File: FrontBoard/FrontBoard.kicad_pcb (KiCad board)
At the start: 2 copper layers, 0 parts

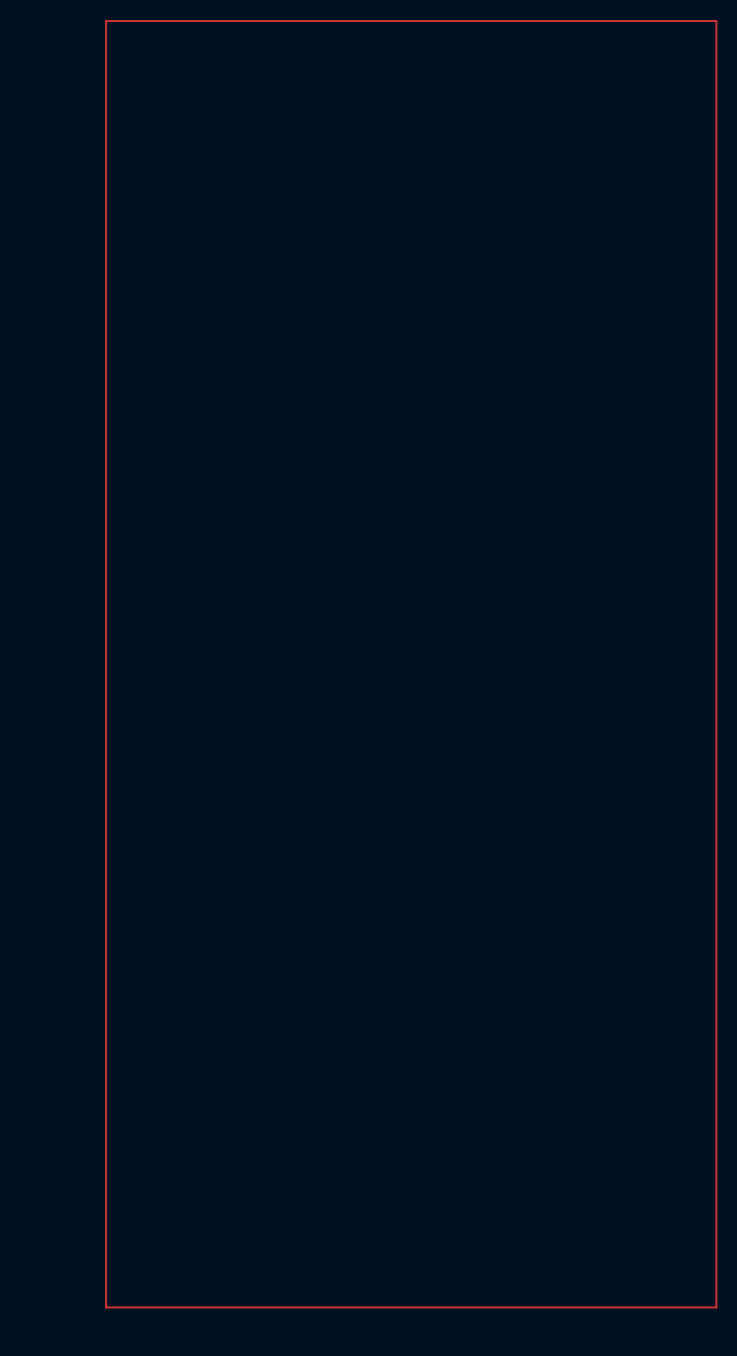
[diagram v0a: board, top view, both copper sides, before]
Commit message: added footprints and 3dmodels
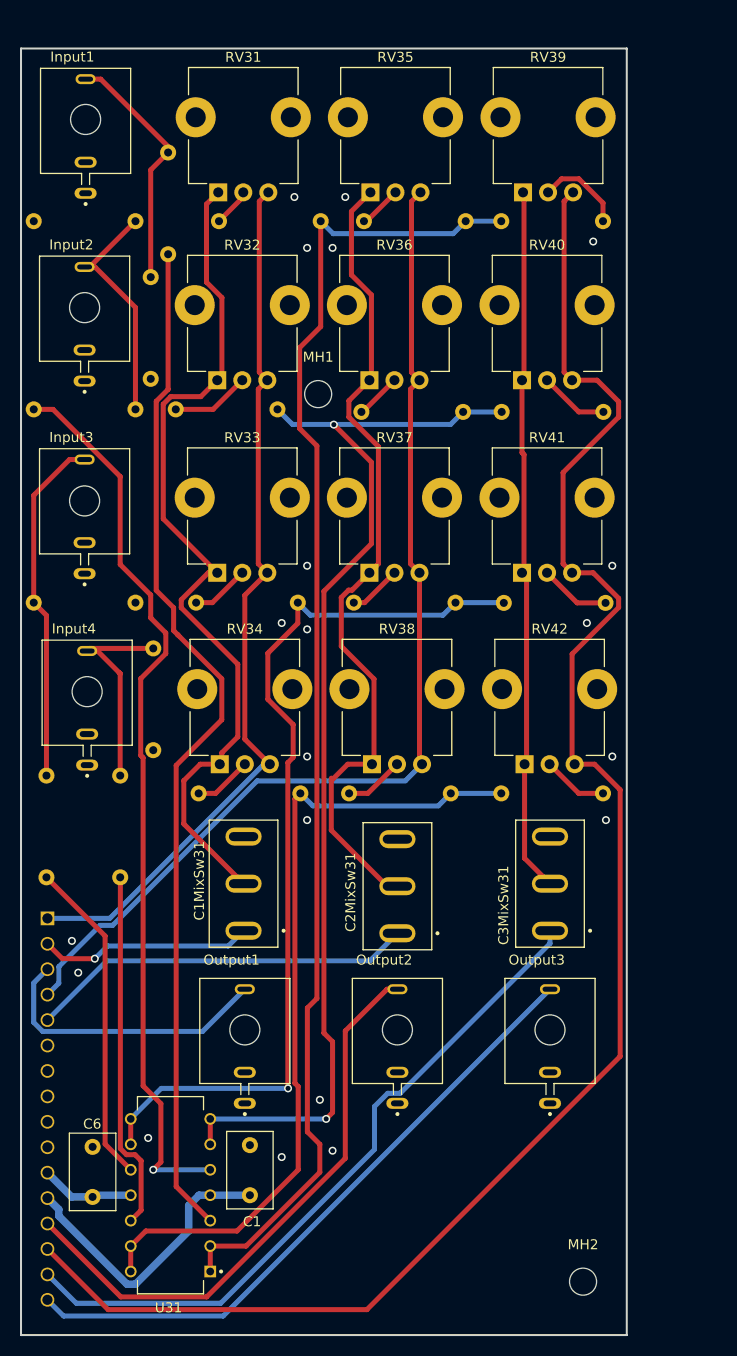
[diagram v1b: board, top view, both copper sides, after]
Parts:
- added C1: 0.1uf, Capacitor_THT:C_Disc_D7.5mm_W4.4mm_P5.00mm, F.Cu at (124.4, 147.0)
- added C1MixSw31: SW_SPDT, 100SP1T6B11M1REH:SW_100SP1T6B11M1REH, F.Cu at (123.7, 115.9)
- added C2MixSw31: SW_SPDT, 100SP1T6B11M1REH:SW_100SP1T6B11M1REH, F.Cu at (139.1, 116.2)
- added C3MixSw31: SW_SPDT, 100SP1T6B11M1REH:SW_100SP1T6B11M1REH, F.Cu at (154.3, 115.9)
- added C6: 0.1uf, Capacitor_THT:C_Disc_D7.5mm_W4.4mm_P5.00mm, F.Cu at (108.6, 147.2)
- added Input1: PJ398SM-12, PJ398SM:THONK_PJ398SM-12, F.Cu at (108.0, 40.5)
- added Input2: PJ398SM-12, PJ398SM:THONK_PJ398SM-12, F.Cu at (107.8, 59.2)
- added Input3: PJ398SM-12, PJ398SM:THONK_PJ398SM-12, F.Cu at (107.8, 78.5)
- added Input4: PJ398SM-12, PJ398SM:THONK_PJ398SM-12, F.Cu at (108.1, 97.6)
- added J1: ESQ-116-33-L-S, ESQ-116-33-L-S:SAMTEC_ESQ-116-33-L-S, B.Cu at (104.1, 119.4)
- added MH1: MountingHole_2.7mm_M2.5, MountingHole:MountingHole_2.7mm_M2.5, F.Cu at (131.2, 67.0)
- added MH2: MountingHole_2.7mm_M2.5, MountingHole:MountingHole_2.7mm_M2.5, F.Cu at (157.6, 155.7)
- added Output1: PJ398SM-12, PJ398SM:THONK_PJ398SM-12, F.Cu at (123.9, 131.4)
- added Output2: PJ398SM-12, PJ398SM:THONK_PJ398SM-12, F.Cu at (139.1, 131.4)
- added Output3: PJ398SM-12, PJ398SM:THONK_PJ398SM-12, F.Cu at (154.3, 131.4)
- added R33: 100k, Resistor_THT:R_Axial_DIN0207_L6.3mm_D2.5mm_P10.16mm_Horizontal, B.Cu at (131.4, 49.7)
- added R34: 100k, Resistor_THT:R_Axial_DIN0207_L6.3mm_D2.5mm_P10.16mm_Horizontal, B.Cu at (127.1, 68.5)
- added R35: 100k, Resistor_THT:R_Axial_DIN0207_L6.3mm_D2.5mm_P10.16mm_Horizontal, B.Cu at (129.1, 87.8)
- added R36: 100k, Resistor_THT:R_Axial_DIN0207_L6.3mm_D2.5mm_P10.16mm_Horizontal, B.Cu at (129.4, 106.9)
- added R37: 100k, Resistor_THT:R_Axial_DIN0207_L6.3mm_D2.5mm_P10.16mm_Horizontal, B.Cu at (145.9, 49.7)
- added R38: 100k, Resistor_THT:R_Axial_DIN0207_L6.3mm_D2.5mm_P10.16mm_Horizontal, B.Cu at (145.7, 68.8)
- added R39: 100k, Resistor_THT:R_Axial_DIN0207_L6.3mm_D2.5mm_P10.16mm_Horizontal, B.Cu at (144.9, 87.8)
- added R40: 100k, Resistor_THT:R_Axial_DIN0207_L6.3mm_D2.5mm_P10.16mm_Horizontal, B.Cu at (144.4, 106.9)
- added R41: 100k, Resistor_THT:R_Axial_DIN0207_L6.3mm_D2.5mm_P10.16mm_Horizontal, B.Cu at (149.5, 49.7)
- added R42: 100k, Resistor_THT:R_Axial_DIN0207_L6.3mm_D2.5mm_P10.16mm_Horizontal, B.Cu at (149.5, 68.8)
- added R43: 100k, Resistor_THT:R_Axial_DIN0207_L6.3mm_D2.5mm_P10.16mm_Horizontal, B.Cu at (149.7, 87.9)
- added R44: 100k, Resistor_THT:R_Axial_DIN0207_L6.3mm_D2.5mm_P10.16mm_Horizontal, B.Cu at (149.5, 106.9)
- added R45: 100k, Resistor_THT:R_Axial_DIN0207_L6.3mm_D2.5mm_P10.16mm_Horizontal, B.Cu at (114.5, 65.5)
- added R46: 100k, Resistor_THT:R_Axial_DIN0207_L6.3mm_D2.5mm_P10.16mm_Horizontal, B.Cu at (102.8, 49.7)
- added R47: 100k, Resistor_THT:R_Axial_DIN0207_L6.3mm_D2.5mm_P10.16mm_Horizontal, B.Cu at (112.9, 87.8)
- added R48: 100k, Resistor_THT:R_Axial_DIN0207_L6.3mm_D2.5mm_P10.16mm_Horizontal, B.Cu at (114.7, 102.6)
- added R49: 1k, Resistor_THT:R_Axial_DIN0207_L6.3mm_D2.5mm_P10.16mm_Horizontal, B.Cu at (116.2, 42.9)
- added R50: 1k, Resistor_THT:R_Axial_DIN0207_L6.3mm_D2.5mm_P10.16mm_Horizontal, B.Cu at (112.9, 68.5)
- added R51: 1k, Resistor_THT:R_Axial_DIN0207_L6.3mm_D2.5mm_P10.16mm_Horizontal, B.Cu at (104.0, 105.1)
- added R52: 1k, Resistor_THT:R_Axial_DIN0207_L6.3mm_D2.5mm_P10.16mm_Horizontal, B.Cu at (111.4, 105.1)
- added REF**: MountingHole_3mm, MountingHole:MountingHole_3mm, F.Cu at (107.8, 77.7)
- added REF**: MountingHole_3mm, MountingHole:MountingHole_3mm, F.Cu at (108.0, 39.6)
- added REF**: MountingHole_3mm, MountingHole:MountingHole_3mm, F.Cu at (108.1, 96.7)
- added REF**: MountingHole_3mm, MountingHole:MountingHole_3mm, F.Cu at (154.3, 130.5)
- added REF**: MountingHole_3mm, MountingHole:MountingHole_3mm, F.Cu at (123.9, 130.5)
- added REF**: MountingHole_3mm, MountingHole:MountingHole_3mm, F.Cu at (139.1, 130.5)
- added REF**: MountingHole_3mm, MountingHole:MountingHole_3mm, F.Cu at (107.8, 58.4)
- added RV31: 20k, Potentiometer_THT:Potentiometer_TT_P0915N, F.Cu at (121.2, 46.9)
- added RV32: 20k, Potentiometer_THT:Potentiometer_TT_P0915N, F.Cu at (121.1, 65.6)
- added RV33: 20k, Potentiometer_THT:Potentiometer_TT_P0915N, F.Cu at (121.1, 84.9)
- added RV34: 20k, Potentiometer_THT:Potentiometer_TT_P0915N, F.Cu at (121.4, 104.0)
- added RV35: 20k, Potentiometer_THT:Potentiometer_TT_P0915N, F.Cu at (136.4, 46.9)
- added RV36: 20k, Potentiometer_THT:Potentiometer_TT_P0915N, F.Cu at (136.3, 65.6)
- added RV37: 20k, Potentiometer_THT:Potentiometer_TT_P0915N, F.Cu at (136.3, 84.9)
- added RV38: 20k, Potentiometer_THT:Potentiometer_TT_P0915N, F.Cu at (136.6, 104.0)
- added RV39: 20k, Potentiometer_THT:Potentiometer_TT_P0915N, F.Cu at (151.6, 46.9)
- added RV40: 20k, Potentiometer_THT:Potentiometer_TT_P0915N, F.Cu at (151.5, 65.6)
- added RV41: 20k, Potentiometer_THT:Potentiometer_TT_P0915N, F.Cu at (151.5, 84.9)
- added RV42: 20k, Potentiometer_THT:Potentiometer_TT_P0915N, F.Cu at (151.8, 104.0)
- added U31: TL074CN, TL074CN:DIP794W45P254L1969H508Q14, F.Cu at (116.4, 147.0)
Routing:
- net C3MixLadderOut: track 0.00 -> 171.5 mm
- net Signal1: track 0.00 -> 133.1 mm
- net Signal2: track 0.00 -> 111.2 mm, vias 0 -> 2
- net C2MixLadderOut: track 0.00 -> 106.6 mm
- net Net-(U31-1IN+): track 0.00 -> 103.2 mm
- net Signal3: track 0.00 -> 92.7 mm, vias 0 -> 1
- net Net-(U31-2IN+): track 0.00 -> 90.4 mm, vias 0 -> 1
- net C1MixLadderOut: track 0.00 -> 89.1 mm
- net Net-(C1MixSw31-B): track 0.00 -> 87.0 mm
- net Net-(C2MixSw31-B): track 0.00 -> 82.9 mm
- net Signal4: track 0.00 -> 81.5 mm
- net Net-(C3MixSw31-B): track 0.00 -> 70.7 mm
- net C3MixModeOut: track 0.00 -> 69.4 mm
- net C3MixOut: track 0.00 -> 64.4 mm
- net C2MixOut: track 0.00 -> 58.2 mm
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- added copper zone on In1.Cu, net GND
- added copper zone on In2.Cu, net GND
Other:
- board outline added: 60.5 x 128.5 mm
- copper layers 2 -> 4

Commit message: updated 200 ohm resister on output to 1k for more reverse protection
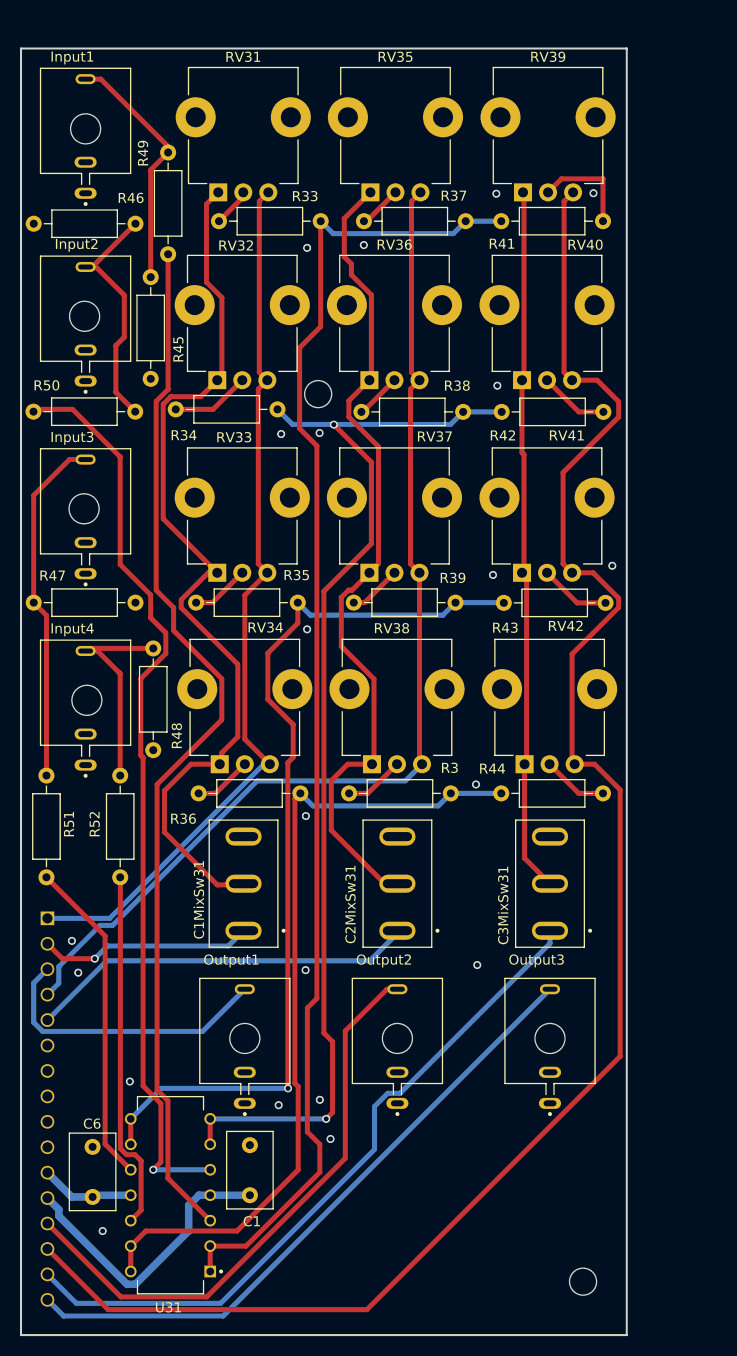
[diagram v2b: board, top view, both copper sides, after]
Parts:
- Input4_PCBH, Input_PCBH, Output1_PCBH, Output2_PCBH, Output3_PCBH: renamed from REF**; moved to B.Cu
- MH1, MH2: moved to B.Cu
- R3: renamed from R40; moved to F.Cu
- R33, R34, R35, R36, R37, R38, R39, R41, R42, R43, R44, R45, R46, R47, R48, R49, R50, R51, R52: moved to F.Cu
- moved Input_PCBH 0.94 mm to (108.0, 40.5), turned to 180 degrees
- moved Input4_PCBH 0.86 mm to (108.1, 97.6), turned to 180 degrees
- moved Input2_PCBH 0.86 mm to (107.8, 59.2)
- moved Output1_PCBH 0.86 mm to (123.9, 131.4), turned to 180 degrees
- moved Output2_PCBH 0.86 mm to (139.1, 131.4), turned to 180 degrees
- moved Output3_PCBH 0.86 mm to (154.3, 131.4), turned to 180 degrees
- moved Input3_PCBH 0.79 mm to (107.8, 78.5)
- moved C2MixSw31 0.25 mm to (139.1, 115.9)
- moved R46 0.25 mm to (102.8, 50.0)
- moved R50 0.23 mm to (112.9, 68.8)
- moved Input4 0.15 mm to (108.0, 97.6)
- moved Input2 0.10 mm to (108.0, 59.2)
- moved Input3 0.10 mm to (108.0, 78.5)
- turned MH1 to 180 degrees
- turned MH2 to 180 degrees
- renumbered REF** to Input2_PCBH, REF** to Input3_PCBH
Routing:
- net Net-(C1MixSw31-B): track 87.0 -> 90.7 mm
- net Net-(R41-Pad2): track 8.86 -> 10.3 mm
- net Net-(U31-1IN+): track 103.2 -> 104.6 mm
- net Net-(U31-2IN+): track 90.4 -> 91.7 mm
- net Net-(Input2-Pad3): track 23.9 -> 24.6 mm
- net GND: vias 20 -> 21

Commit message: replaced SPST swtiches with sub-toggle, alinged switch faceplace holes, updated 3d models
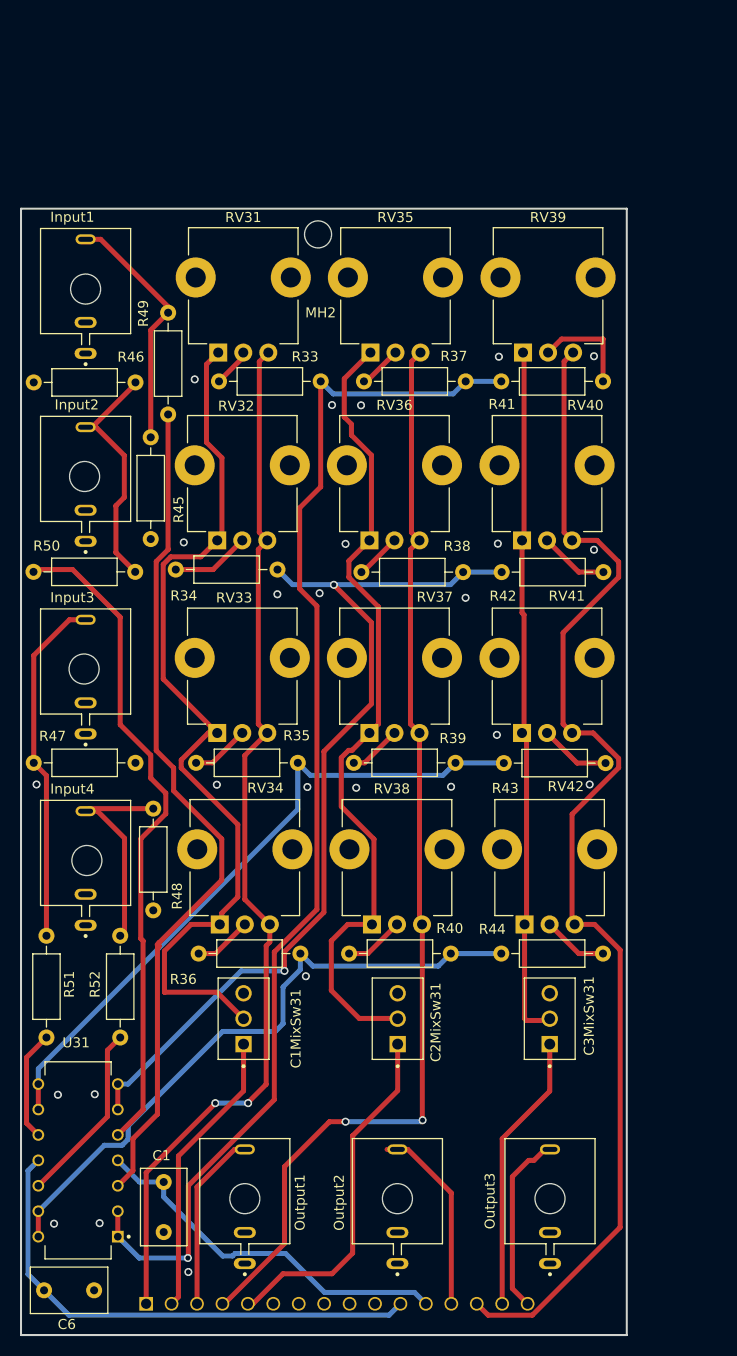
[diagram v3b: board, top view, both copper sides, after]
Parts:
- removed the MH2 at (157.6, 155.7)
- C1MixSw31, C2MixSw31, C3MixSw31: footprint 100SP1T6B11M1REH:SW_100SP1T6B11M1REH -> 2MS1T1B1M2QES:SW_2MS1T1B1M2QES
- MH2: renamed from MH1; moved to F.Cu
- moved J1 39.7 mm to (114.0, 157.9), turned to 0 degrees
- moved Input2_PCBH 16.0 mm to (107.8, 75.2)
- moved R33 16.0 mm to (131.4, 65.7)
- moved R37 16.0 mm to (145.9, 65.7)
- moved R41 16.0 mm to (149.5, 65.7)
- moved Input1 16.0 mm to (108.0, 56.5)
- moved Input3 16.0 mm to (108.0, 94.5)
- moved Input3_PCBH 16.0 mm to (107.8, 94.5)
- moved Input4 16.0 mm to (108.0, 113.6)
- moved Input4_PCBH 16.0 mm to (108.1, 113.6)
- moved Input_PCBH 16.0 mm to (108.0, 56.5)
- moved Output1 16.0 mm to (123.9, 147.4)
- moved Output1_PCBH 16.0 mm to (123.9, 147.4)
- moved Output2 16.0 mm to (139.1, 147.4)
- moved Output2_PCBH 16.0 mm to (139.1, 147.4)
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- renumbered R3 to R40
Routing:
- net C3MixLadderOut: track 171.5 -> 120.8 mm
- net C3MixOut: track 64.4 -> 18.2 mm
- net -v: track 9.39 -> 51.2 mm
- net C3MixModeOut: track 69.4 -> 27.7 mm
- net C2MixOut: track 58.2 -> 19.3 mm
- net Signal3: track 92.7 -> 67.0 mm, vias 1 -> 0
- net Net-(U31-2IN+): track 91.7 -> 66.5 mm, vias 1 -> 0
- net Net-(U31-3IN+): track 32.7 -> 11.0 mm
- net Signal2: track 111.2 -> 91.2 mm
- net Net-(U31-1IN+): track 104.6 -> 84.8 mm
- net Net-(U31-4IN+): track 36.1 -> 18.2 mm
- net Signal4: track 81.5 -> 64.3 mm
- net C1MixLadderOut: track 89.1 -> 106.2 mm, vias 0 -> 2
- net C1MixOut: track 29.1 -> 18.0 mm
- net Signal1: track 133.1 -> 124.1 mm, vias 0 -> 1
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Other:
- board size 60.5 x 128.5 mm -> 60.5 x 112.5 mm
- board text added: "R-mods"
- board text added: "RM-MMB2-2024-v1.0.0"
